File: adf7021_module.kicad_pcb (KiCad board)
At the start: 4 copper layers, 52 x 44 mm, 77 parts, among them J1 Conn_02x10_Counter_Clockwise, J2 Conn_Coaxial, J3 Conn_Coaxial, J4 Conn_02x10_Counter_Clockwise, U1 ADF7021, X1 19.68MHz

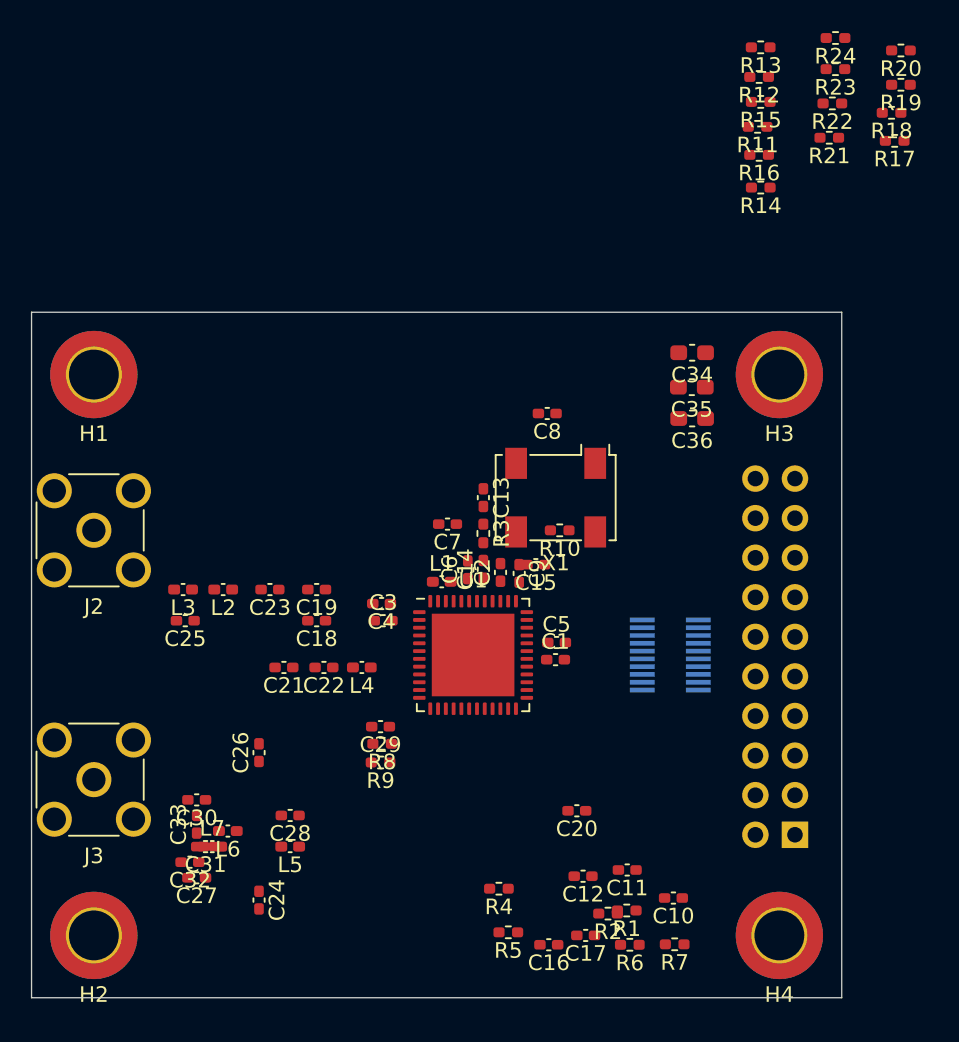
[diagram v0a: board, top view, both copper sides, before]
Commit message: some component placement attempts
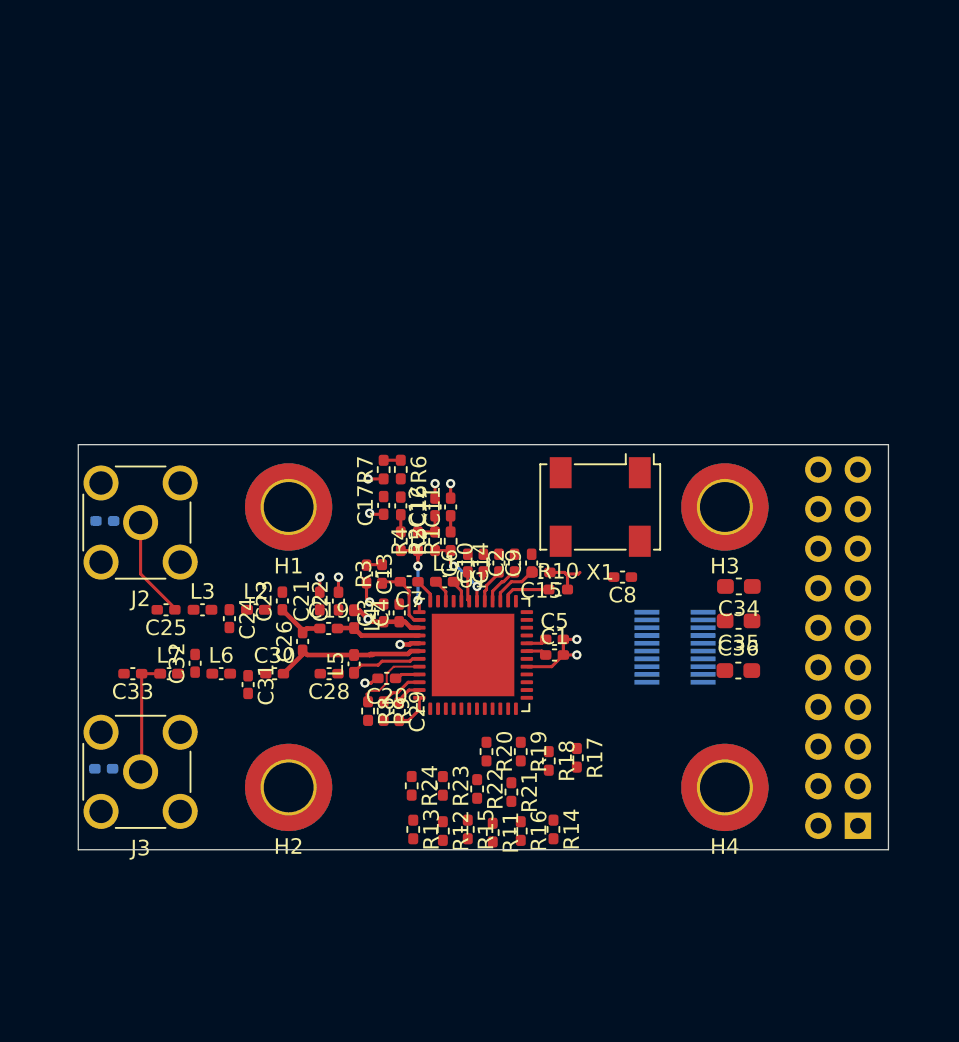
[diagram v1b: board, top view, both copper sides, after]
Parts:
- C18, C27: moved to B.Cu
- moved R24 55.2 mm to (127.4, 66.4), turned to 270 degrees
- moved R13 54.9 mm to (127.5, 69.2), turned to 270 degrees
- moved R12 52.5 mm to (129.4, 69.3), turned to 270 degrees
- moved R23 52.5 mm to (129.4, 66.4), turned to 270 degrees
- moved R20 52.3 mm to (132.2, 64.2), turned to 270 degrees
- moved R15 50.3 mm to (131.0, 69.2), turned to 270 degrees
- moved R22 49.6 mm to (131.6, 66.6), turned to 270 degrees
- moved R19 49.3 mm to (134.4, 64.2), turned to 270 degrees
- moved R11 48.4 mm to (132.6, 69.4), turned to 270 degrees
- moved R18 47.1 mm to (136.2, 64.8), turned to 270 degrees
- moved R21 46.7 mm to (133.8, 66.8), turned to 270 degrees
- moved R16 46.0 mm to (134.4, 69.3), turned to 270 degrees
- moved R17 44.5 mm to (138.0, 64.6), turned to 270 degrees
- moved R14 43.3 mm to (136.5, 69.2), turned to 270 degrees
- moved R7 35.7 mm to (125.6, 46.1), turned to 90 degrees
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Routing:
- net GND: track 0.00 -> 17.9 mm, vias 0 -> 11
- net +3V3: track 0.00 -> 12.2 mm, vias 0 -> 1
- net /RFIN: track 0.00 -> 10.1 mm
- net Net-(C27-Pad2): track 0.00 -> 7.41 mm
- net Net-(C18-Pad1): track 0.00 -> 6.51 mm
- net /CPOUT: track 0.00 -> 6.48 mm, vias 0 -> 2
- net /VCOIN: track 0.00 -> 5.59 mm, vias 0 -> 2
- net /RFOUT: track 0.00 -> 5.46 mm
- net /R_LNA: track 0.00 -> 4.97 mm
- net Net-(C28-Pad1): track 0.00 -> 4.59 mm
- net /CREG1: track 0.00 -> 4.36 mm
- net Net-(C19-Pad1): track 0.00 -> 3.21 mm
- net Net-(R10-Pad1): track 0.00 -> 3.18 mm
- net Net-(C15-Pad2): track 0.00 -> 3.11 mm
- net CLK_IN: track 0.00 -> 3.06 mm
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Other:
- board size 52 x 44 mm -> 52 x 26 mm
- net class Default: via_dia 0.8 -> 0.6; via_drill 0.4 -> 0.3
- board text added: "12mil / 0.3mm trace should be 50Ωish"
- board text removed: "6mil / 0.15mm trace should be 50Ωish"

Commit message: some more layout attempts
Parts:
- removed R11, R12, R15, R16, R17, R18, R19, R20, R21, R22, R23, R24: 22, Resistor_SMD:R_0402_1005Metric_Pad0.72x0.64mm_HandSolder
- added RN1: 22, Resistor_SMD:R_Array_Concave_4x0402, F.Cu at (136.9, 57.0)
- added RN2: 22, Resistor_SMD:R_Array_Concave_4x0402, B.Cu at (146.1, 57.7)
- added RN3: 22, Resistor_SMD:R_Array_Concave_4x0402, F.Cu at (148.7, 57.7)
- H1, H2, H3, H4: footprint MountingHole:MountingHole_3.2mm_M3_DIN965_Pad_TopBottom -> MountingHole:MountingHole_2.2mm_M2_Pad_TopBottom
- R13: value 22 -> 1k
- moved J4 23.3 mm to (151.9, 46.0), turned to 180 degrees
- moved R13 17.9 mm to (138.1, 54.8), turned to 180 degrees
- moved C34 16.0 mm to (140.5, 67.5), turned to 90 degrees
- moved C35 15.1 mm to (138.8, 67.5), turned to 90 degrees
- moved C36 14.2 mm to (137.0, 67.5), turned to 90 degrees
- moved R14 8.19 mm to (139.3, 61.5), turned to 180 degrees
- moved C8 4.57 mm to (141.0, 48.4), turned to 90 degrees
- moved X1 3.30 mm to (136.2, 48.5)
- moved C1 2.85 mm to (137.1, 60.8), turned to 270 degrees
- moved C23 2.44 mm to (120.5, 56.5)
- moved J1 2.40 mm to (141.9, 57.5)
- moved C5 2.20 mm to (136.6, 59.2)
- moved C10 2.00 mm to (132.0, 54.1)
- moved C11 2.00 mm to (129.9, 50.5)
- moved C12 2.00 mm to (128.9, 50.5)
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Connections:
- J1 pad 1: +3V3 -> CLK_IN
- J1 pad 10: CLK_IN -> +3V3
- J1 pad 2: FM_MOD -> GND
- J1 pad 3: Net-(J1-Pad3) -> GND
- J1 pad 5: GND -> Net-(J1-Pad5)
- J1 pad 6: Net-(J1-Pad6) -> GND
- J1 pad 8: GND -> Net-(J1-Pad8)
- J1 pad 9: GND -> FM_MOD
- J4 pad 1: +3V3 -> CLK_IN
- J4 pad 10: CLK_IN -> SREAD
- J4 pad 11: CLKOUT -> GND
- J4 pad 13: TxRxCLK -> Net-(J4-Pad13)
- J4 pad 14: TxRxData -> MUXOUT
- J4 pad 15: SREAD -> Net-(J4-Pad15)
- J4 pad 16: GND -> SWD
- J4 pad 17: MUXOUT -> FM_MOD
- J4 pad 18: SWD -> ADCIN
- J4 pad 19: ADCIN -> +3V3
- J4 pad 2: FM_MOD -> CLKOUT
- J4 pad 3: Net-(J4-Pad3) -> GND
- J4 pad 4: Net-(J4-Pad4) -> GND
- J4 pad 6: Net-(J4-Pad6) -> TxRxCLK
- J4 pad 8: GND -> TxRxData
- J4 pad 9: GND -> Net-(J4-Pad9)
- R13 pad 1: SREAD -> CLKOUT
- R14 pad 1: SWD -> SREAD
- U1 pad 27: Net-(R13-Pad2) -> Net-(R14-Pad2)
- U1 pad 33: Net-(R14-Pad2) -> Net-(RN1-Pad4)
- U1 pad 36: Net-(R16-Pad2) -> Net-(R13-Pad2)
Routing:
- net SCLK: track 0.00 -> 17.8 mm, vias 0 -> 1
- net SDATA: track 0.00 -> 17.2 mm, vias 0 -> 1
- net CE: track 0.00 -> 17.2 mm, vias 0 -> 1
- net SLE: track 0.00 -> 16.6 mm, vias 0 -> 1
- net FM_MOD: track 1.10 -> 12.5 mm, vias 0 -> 1
- net Net-(J4-Pad15): track 0.00 -> 7.02 mm
- net MUXOUT: track 0.00 -> 5.79 mm, vias 0 -> 1
- net Net-(J4-Pad13): track 0.00 -> 4.73 mm
- net Net-(J4-Pad7): track 0.00 -> 4.61 mm
- net Net-(C9-Pad2): track 0.00 -> 4.04 mm
- net CLKOUT: track 0.00 -> 3.75 mm, vias 0 -> 1
- net Net-(C19-Pad1): track 3.21 -> 6.28 mm
- net SWD: track 0.00 -> 3.04 mm, vias 0 -> 1
- net Net-(RN1-Pad1): track 0.00 -> 2.97 mm
- net Net-(J4-Pad9): track 0.00 -> 2.94 mm
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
